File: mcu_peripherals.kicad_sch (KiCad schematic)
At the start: 85 parts, among them J2 USB_C_Receptacle_USB2.0_16P, J3 Conn_01x05, J4 Micro_SD_Card_Det_Hirose_DM3AT, SW1 RESET, SW2 BOOT, U12 USBLC6-2SC6, U14 TPS3840DL42DBVR, U15 ATECC608B-SSHDA, U16 USBLC6-2SC6, U17 ASM330LHHTR, U18 TCA9535PWR, U20 W25N01GVZEIG, U23 TPS22918TDBVTQ1, U802 TMP1075DGKR, U902 SN74AXC4T245QPWRQ1, U903 SN74AXC4T245QPWRQ1

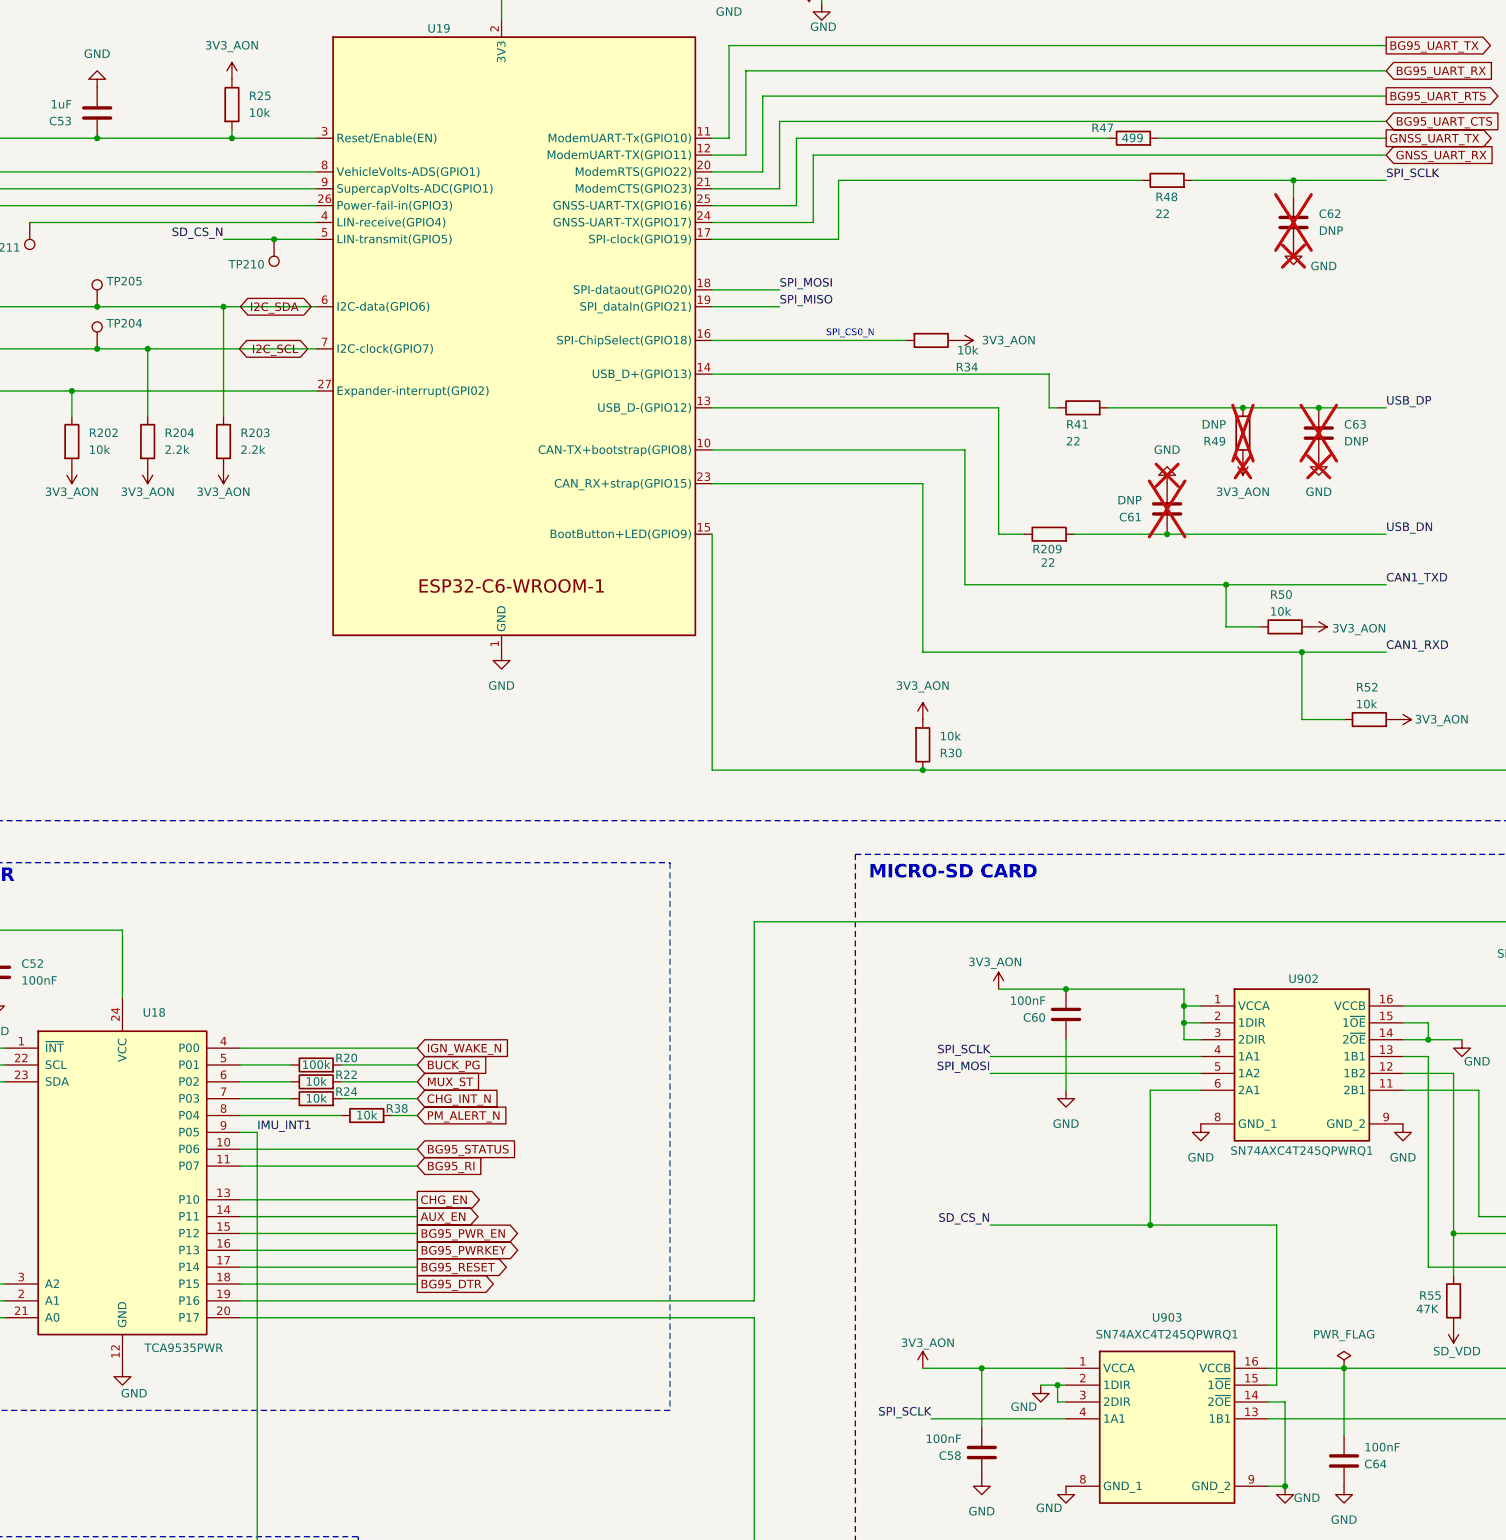
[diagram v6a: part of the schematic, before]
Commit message: Adjust BG95 SPI and power net wiring
This schematic update adds the BG95_PG signal and related junctions/wires, fixes the SPI net naming and routing, and updates the associated power/ground symbols and testpoint placement. It also changes a resistor value, removes obsolete resistor instances, and refreshes designator usage in the KiCad project files to match the current sheet state.
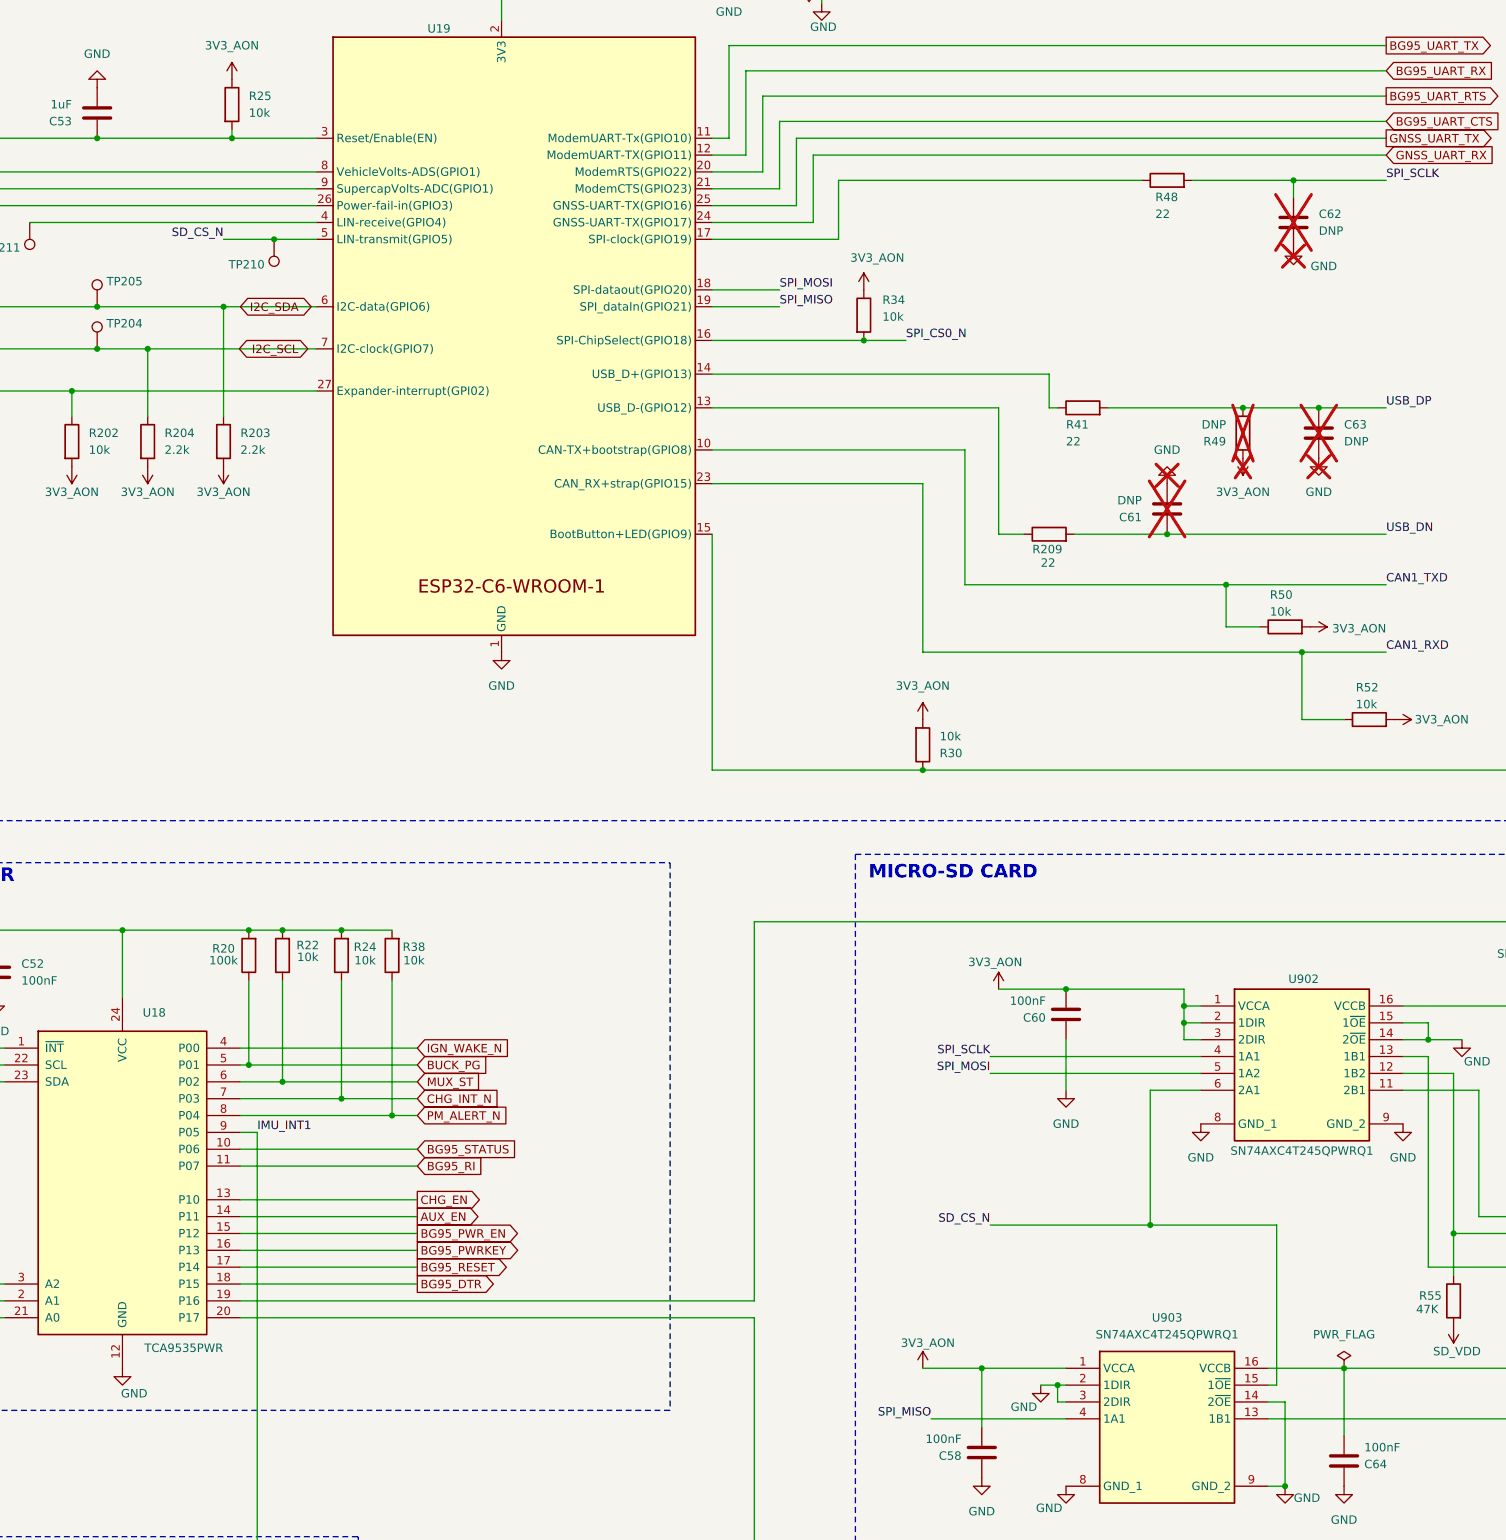
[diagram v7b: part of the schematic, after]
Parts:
- removed R47: 499, symbol Device:R
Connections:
- net 3V3_AON: now also R20.2, R22.2, R24.2, R38.2
- net BUCK_PG: now also R20.1, U18.5 (P01); no longer R20.2
- net CHG_INT_N: now also R24.1, U18.7 (P03); no longer R24.2
- net GNSS_UART_TX: now also U19.25 (GNSS-UART-TX(GPIO16))
- net MUX_ST: now also R22.1, U18.6 (P02); no longer R22.2
- net PM_ALERT_N: now also R38.1, U18.8 (P04); no longer R38.2
- net SPI_CS0_N: now also R34.2, U19.16 (SPI-ChipSelect(GPIO18))
- net SPI_MISO: now also U903.4 (1A1)
- net SPI_SCLK: no longer U903.4 (1A1)
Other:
- note removed: "SPI_CS0_N"
- moved on the sheet: R34

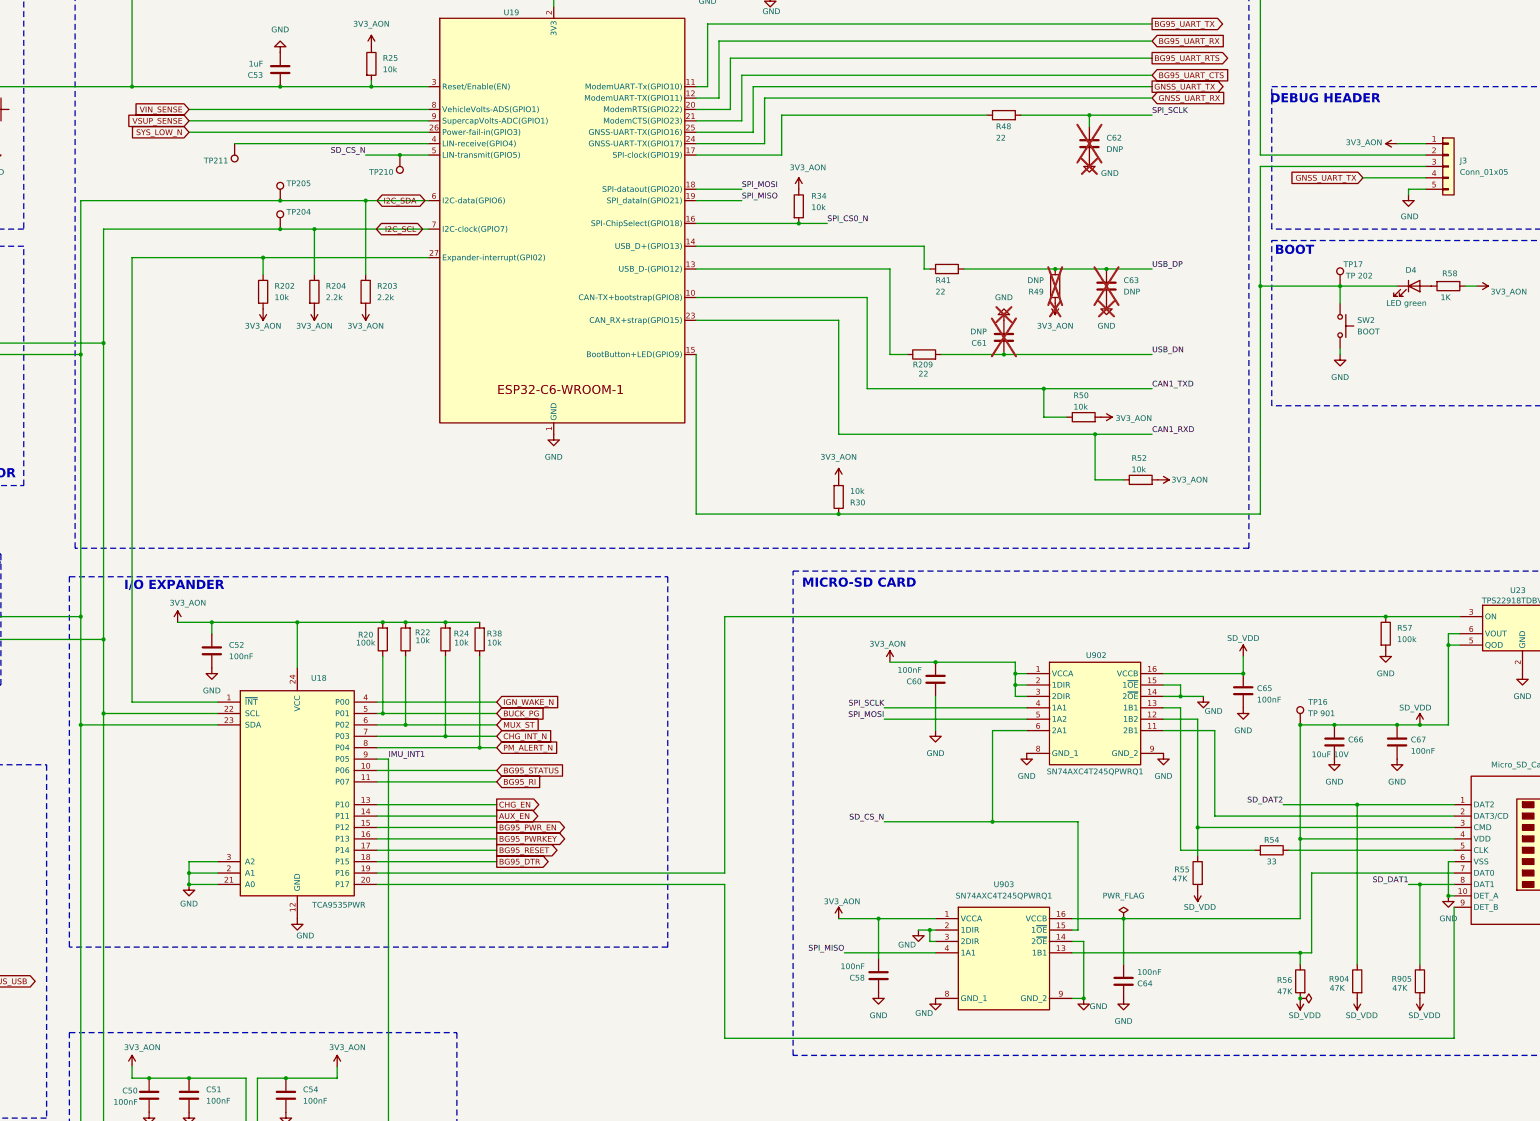
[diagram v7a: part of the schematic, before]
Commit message: Fix MCU net labels and passive values
This schematic update corrects a mislabeled power net from VSYS to 3V3_AON and fixes several capacitor values in the cellular path from nF to pF. It also reworks the MCU peripheral net/junction layout and adds the associated resistor references to match the intended signal routing and designators.
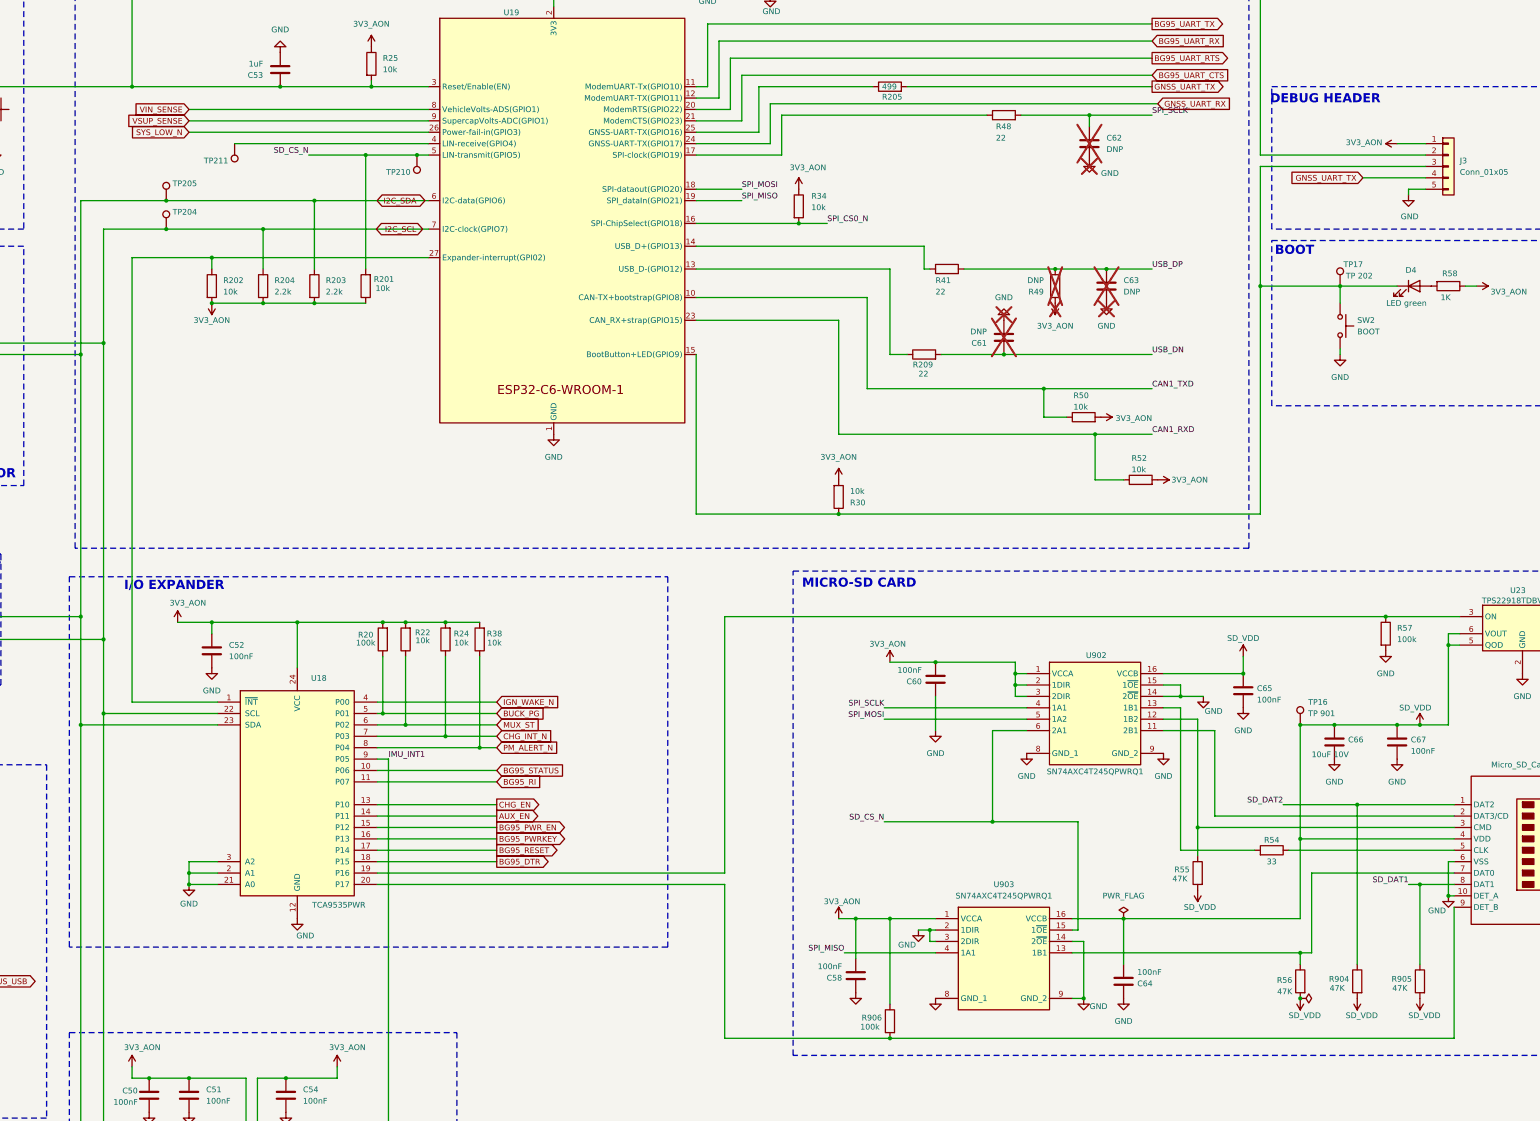
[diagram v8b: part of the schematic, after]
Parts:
- added R201: 10k, symbol Device:R
- added R205: 499, symbol Device:R
- added R906: 100k, symbol Device:R
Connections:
- net 3V3_AON: now also R201.1, R906.1
- net GNSS_UART_TX: now also R205.2; no longer U19.25 (GNSS-UART-TX(GPIO16))
- net SD_CS_N: now also R201.2
- net at J4.9 (DET_B), U18.20 (P17): now also R906.2
- new net: R205.1, U19.25 (GNSS-UART-TX(GPIO16))
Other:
- moved on the sheet: C58, R202, R203, R204, TP204, TP205, TP210
